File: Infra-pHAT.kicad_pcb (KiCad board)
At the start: 2 copper layers, 65 x 30 mm, 24 parts, among them Q1 BC817, U1 CAT24C32WI-GT3

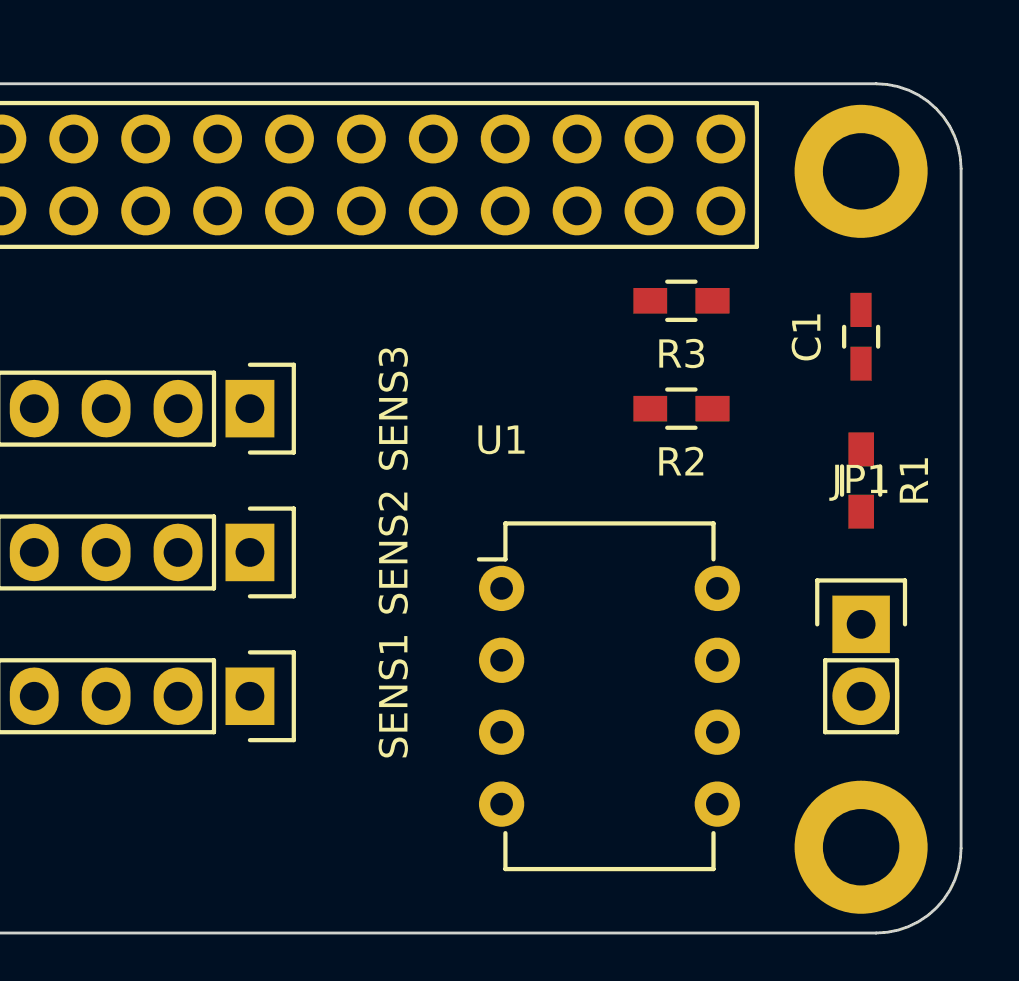
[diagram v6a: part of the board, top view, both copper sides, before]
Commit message: Infra-pHAT.kicad_pcb: Route EEPROM
Signed-off-by: Leon Anavi <leon@anavi.org>
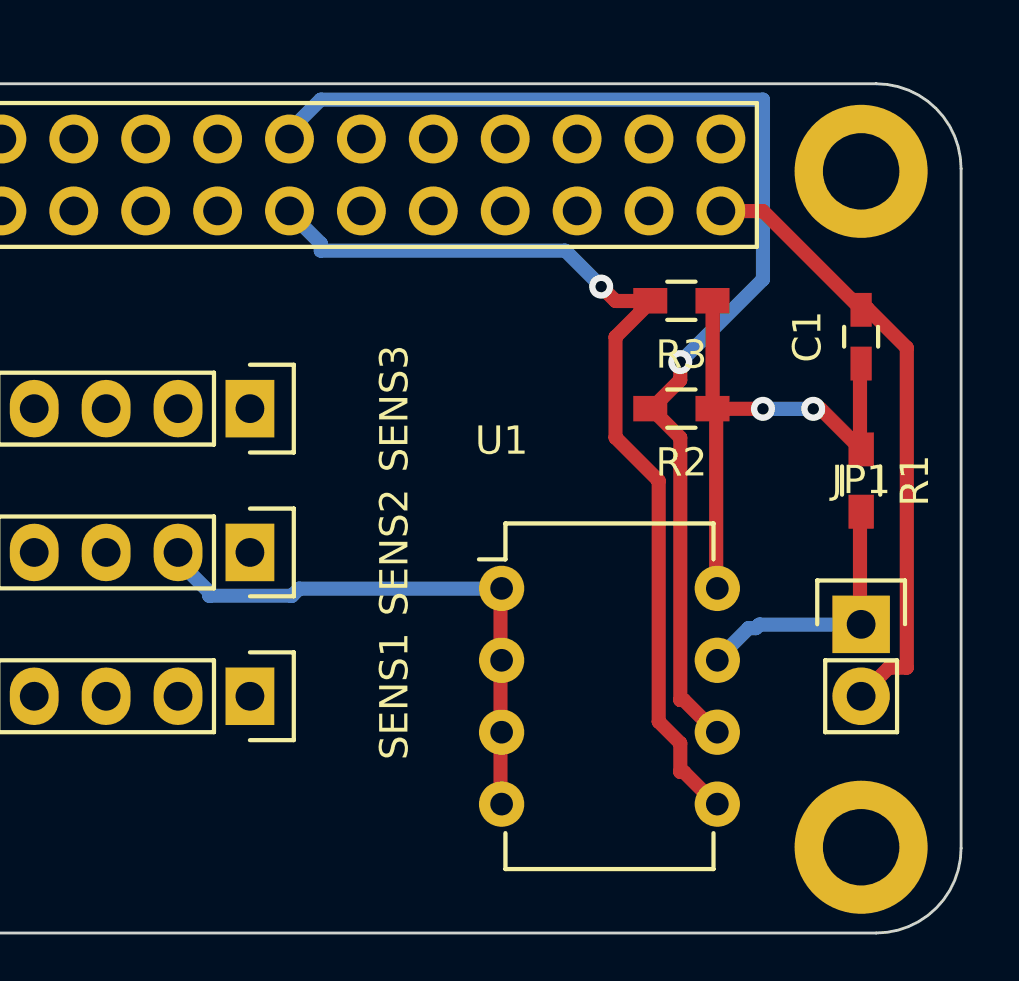
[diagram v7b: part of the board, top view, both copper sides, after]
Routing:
- net Net-(R2-Pad2): track 0.00 -> 42.7 mm, vias 0 -> 1
- net GND: track 0.00 -> 42.5 mm
- net Net-(R3-Pad2): track 0.00 -> 34.3 mm, vias 0 -> 1
- net +3V3: track 0.00 -> 19.3 mm, vias 0 -> 2
- net Net-(JP1-Pad1): track 0.00 -> 9.73 mm
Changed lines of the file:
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@@
   (general
     (links 59)
-    (no_connects 59)
-    (area 136.875429 73.719 225.152572 106.453)
+    (no_connects 43)
+    (area 136.779 73.66 225.171 106.426)
     (thickness 1.6)
     (drawings 13)
-    (tracks 0)
+    (tracks 90)
     (zones 0)
     (modules 24)
@@
   (gr_arc (start 151.5011 102.0036) (end 148.5011 102.0036) (angle -90) (layer Edge.Cuts) (width 0.1))
   (gr_circle (center 152.0011 101.5036) (end 152.0011 101.5036) (layer Edge.Cuts) (width 0.1))
+  (segment (start 204.72 86.48) (end 204.724 86.487) (width 0.5) (layer F.Cu) (net 1) (status 80000))
+  (segment (start 204.724 86.487) (end 204.724 82.677) (width 0.5) (layer F.Cu) (net 1) (status 80000))
+  (segment (start 204.724 82.677) (end 204.72 82.67) (width 0.5) (layer F.Cu) (net 1) (status 80000))
+  (segment (start 204.72 86.48) (end 204.724 86.487) (width 0.5) (layer F.Cu) (net 1) (status 80000))
+  (segment (start 204.724 86.487) (end 206.502 86.487) (width 0.5) (layer F.Cu) (net 1) (status 80000))
+  (via (at 206.502 86.487) (size 0.85) (layers F.Cu B.Cu) (net 1) (status 80000))
+  (segment (start 206.502 86.487) (end 208.28 86.487) (width 0.5) (layer B.Cu) (net 1) (status 80000))
+  (via (at 208.28 86.487) (size 0.85) (layers F.Cu B.Cu) (net 1) (status 80000))
+  (segment (start 208.28 86.487) (end 208.534 86.487) (width 0.5) (layer F.Cu) (net 1) (status 80000))
+  (segment (start 208.534 86.487) (end 209.931 87.884) (width 0.5) (layer F.Cu) (net 1) (status 80000))
+  (segment (start 209.931 87.884) (end 209.97 87.92) (width 0.5) (layer F.Cu) (net 1) (status 80000))
+  (segment (start 209.97 87.92) (end 209.931 87.884) (width 0.5) (layer F.Cu) (net 1) (status 80000))
+  (segment (start 209.931 87.884) (end 209.931 84.836) (width 0.5) (layer F.Cu) (net 1) (status 80000))
+  (segment (start 209.931 84.836) (end 209.97 84.89) (width 0.5) (layer F.Cu) (net 1) (status 80000))
+  (segment (start 204.72 86.48) (end 204.724 86.487) (width 0.5) (layer F.Cu) (net 1) (status 80000))
+  (segment (start 204.724 86.487) (end 204.851 86.614) (width 0.5) (layer F.Cu) (net 1) (status 80000))
+  (segment (start 204.851 86.614) (end 204.851 92.837) (width 0.5) (layer F.Cu) (net 1) (status 80000))
+  (segment (start 204.851 92.837) (end 204.89 92.83) (width 0.5) (layer F.Cu) (net 1) (status 80000))
+  (segment (start 205.017 79.495) (end 204.978 79.502) (width 0.5) (layer F.Cu) (net 2) (status 80000))
+  (segment (start 204.978 79.502) (end 206.502 79.502) (width 0.5) (layer F.Cu) (net 2) (status 80000))
+  (segment (start 206.502 79.502) (end 209.931 82.931) (width 0.5) (layer F.Cu) (net 2) (status 80000))
+  (segment (start 209.931 82.931) (end 209.97 82.99) (width 0.5) (layer F.Cu) (net 2) (status 80000))
+  (segment (start 209.97 82.99) (end 209.931 82.931) (width 0.5) (layer F.Cu) (net 2) (status 80000))
+  (segment (start 209.931 82.931) (end 210.185 82.931) (width 0.5) (layer F.Cu) (net 2) (status 80000))
+  (segment (start 210.185 82.931) (end 211.582 84.328) (width 0.5) (layer F.Cu) (net 2) (status 80000))
+  (segment (start 211.582 84.328) (end 211.582 95.631) (width 0.5) (layer F.Cu) (net 2) (status 80000))
+  (segment (start 211.582 95.631) (end 210.947 95.631) (width 0.5) (layer F.Cu) (net 2) (status 80000))
+  (segment (start 210.947 95.631) (end 209.931 96.647) (width 0.5) (layer F.Cu) (net 2) (status 80000))
+  (segment (start 209.931 96.647) (end 209.97 96.64) (width 0.5) (layer F.Cu) (net 2) (status 80000))
+  (segment (start 185.84 91.56) (end 185.801 91.567) (width 0.5) (layer B.Cu) (net 2) (status 80000))
+  (segment (start 185.801 91.567) (end 185.801 91.821) (width 0.5) (layer B.Cu) (net 2) (status 80000))
+  (segment (start 185.801 91.821) (end 186.944 92.964) (width 0.5) (layer B.Cu) (net 2) (status 80000))
+  (segment (start 186.944 92.964) (end 186.944 93.091) (width 0.5) (layer B.Cu) (net 2) (status 80000))
+  (segment (start 186.944 93.091) (end 189.865 93.091) (width 0.5) (layer B.Cu) (net 2) (status 80000))
+  (segment (start 189.865 93.091) (end 190.119 92.837) (width 0.5) (layer B.Cu) (net 2) (status 80000))
+  (segment (start 190.119 92.837) (end 197.231 92.837) (width 0.5) (layer B.Cu) (net 2) (status 80000))
+  (segment (start 197.231 92.837) (end 197.27 92.83) (width 0.5) (layer B.Cu) (net 2) (status 80000))
+  (segment (start 197.27 97.91) (end 197.231 97.917) (width 0.5) (layer F.Cu) (net 2) (status 80000))
+  (segment (start 197.231 97.917) (end 197.231 100.457) (width 0.5) (layer F.Cu) (net 2) (status 80000))
+  (segment (start 197.231 100.457) (end 197.27 100.45) (width 0.5) (layer F.Cu) (net 2) (status 80000))
+  (segment (start 197.27 95.37) (end 197.231 95.377) (width 0.5) (layer F.Cu) (net 2) (status 80000))
+  (segment (start 197.231 95.377) (end 197.231 97.917) (width 0.5) (layer F.Cu) (net 2) (status 80000))
+  (segment (start 197.231 97.917) (end 197.27 97.91) (width 0.5) (layer F.Cu) (net 2) (status 80000))
+  (segment (start 197.27 92.83) (end 197.231 92.837) (width 0.5) (layer F.Cu) (net 2) (status 80000))
+  (segment (start 197.231 92.837) (end 197.231 95.377) (width 0.5) (layer F.Cu) (net 2) (status 80000))
+  (segment (start 197.231 95.377) (end 197.27 95.37) (width 0.5) (layer F.Cu) (net 2) (status 80000))
+  (segment (start 209.97 94.1) (end 209.931 94.107) (width 0.5) (layer F.Cu) (net 6) (status 80000))
+  (segment (start 209.931 94.107) (end 209.931 90.17) (width 0.5) (layer F.Cu) (net 6) (status 80000))
+  (segment (start 209.931 90.17) (end 209.97 90.12) (width 0.5) (layer F.Cu) (net 6) (status 80000))
+  (segment (start 204.89 95.37) (end 204.851 95.377) (width 0.5) (layer B.Cu) (net 6) (status 80000))
+  (segment (start 204.851 95.377) (end 205.994 94.234) (width 0.5) (layer B.Cu) (net 6) (status 80000))
+  (segment (start 205.994 94.234) (end 206.248 94.234) (width 0.5) (layer B.Cu) (net 6) (status 80000))
+  (segment (start 206.248 94.234) (end 206.375 94.107) (width 0.5) (layer B.Cu) (net 6) (status 80000))
+  (segment (start 206.375 94.107) (end 209.931 94.107) (width 0.5) (layer B.Cu) (net 6) (status 80000))
+  (segment (start 209.931 94.107) (end 209.97 94.1) (width 0.5) (layer B.Cu) (net 6) (status 80000))
+  (segment (start 202.52 86.48) (end 202.565 86.487) (width 0.5) (layer F.Cu) (net 8) (status 80000))
+  (segment (start 202.565 86.487) (end 203.581 85.471) (width 0.5) (layer F.Cu) (net 8) (status 80000))
+  (segment (start 203.581 85.471) (end 203.581 84.836) (width 0.5) (layer F.Cu) (net 8) (status 80000))
+  (via (at 203.581 84.836) (size 0.85) (layers F.Cu B.Cu) (net 8) (status 80000))
+  (segment (start 203.581 84.836) (end 206.502 81.915) (width 0.5) (layer B.Cu) (net 8) (status 80000))
+  (segment (start 206.502 81.915) (end 206.502 75.565) (width 0.5) (layer B.Cu) (net 8) (status 80000))
+  (segment (start 206.502 75.565) (end 190.881 75.565) (width 0.5) (layer B.Cu) (net 8) (status 80000))
+  (segment (start 190.881 75.565) (end 189.738 76.708) (width 0.5) (layer B.Cu) (net 8) (status 80000))
+  (segment (start 189.738 76.708) (end 189.738 76.962) (width 0.5) (layer B.Cu) (net 8) (status 80000))
+  (segment (start 189.738 76.962) (end 189.777 76.955) (width 0.5) (layer B.Cu) (net 8) (status 80000))
+  (segment (start 202.52 86.48) (end 202.565 86.487) (width 0.5) (layer F.Cu) (net 8) (status 80000))
+  (segment (start 202.565 86.487) (end 203.581 87.503) (width 0.5) (layer F.Cu) (net 8) (status 80000))
+  (segment (start 203.581 87.503) (end 203.581 96.774) (width 0.5) (layer F.Cu) (net 8) (status 80000))
+  (segment (start 203.581 96.774) (end 203.708 96.774) (width 0.5) (layer F.Cu) (net 8) (status 80000))
+  (segment (start 203.708 96.774) (end 204.851 97.917) (width 0.5) (layer F.Cu) (net 8) (status 80000))
+  (segment (start 204.851 97.917) (end 204.89 97.91) (width 0.5) (layer F.Cu) (net 8) (status 80000))
+  (segment (start 202.52 82.67) (end 202.565 82.677) (width 0.5) (layer F.Cu) (net 9) (status 80000))
+  (segment (start 202.565 82.677) (end 201.295 82.677) (width 0.5) (layer F.Cu) (net 9) (status 80000))
+  (segment (start 201.295 82.677) (end 200.787 82.169) (width 0.5) (layer F.Cu) (net 9) (status 80000))
+  (via (at 200.787 82.169) (size 0.85) (layers F.Cu B.Cu) (net 9) (status 80000))
+  (segment (start 200.787 82.169) (end 199.517 80.899) (width 0.5) (layer B.Cu) (net 9) (status 80000))
+  (segment (start 199.517 80.899) (end 190.881 80.899) (width 0.5) (layer B.Cu) (net 9) (status 80000))
+  (segment (start 190.881 80.899) (end 190.881 80.645) (width 0.5) (layer B.Cu) (net 9) (status 80000))
+  (segment (start 190.881 80.645) (end 189.738 79.502) (width 0.5) (layer B.Cu) (net 9) (status 80000))
+  (segment (start 189.738 79.502) (end 189.777 79.495) (width 0.5) (layer B.Cu) (net 9) (status 80000))
+  (segment (start 202.52 82.67) (end 202.565 82.677) (width 0.5) (layer F.Cu) (net 9) (status 80000))
+  (segment (start 202.565 82.677) (end 201.295 83.947) (width 0.5) (layer F.Cu) (net 9) (status 80000))
+  (segment (start 201.295 83.947) (end 201.295 87.503) (width 0.5) (layer F.Cu) (net 9) (status 80000))
+  (segment (start 201.295 87.503) (end 202.819 89.027) (width 0.5) (layer F.Cu) (net 9) (status 80000))
+  (segment (start 202.819 89.027) (end 202.819 97.536) (width 0.5) (layer F.Cu) (net 9) (status 80000))
+  (segment (start 202.819 97.536) (end 203.581 98.298) (width 0.5) (layer F.Cu) (net 9) (status 80000))
+  (segment (start 203.581 98.298) (end 203.581 99.314) (width 0.5) (layer F.Cu) (net 9) (status 80000))
+  (segment (start 203.581 99.314) (end 203.708 99.314) (width 0.5) (layer F.Cu) (net 9) (status 80000))
+  (segment (start 203.708 99.314) (end 204.851 100.457) (width 0.5) (layer F.Cu) (net 9) (status 80000))
+  (segment (start 204.851 100.457) (end 204.89 100.45) (width 0.5) (layer F.Cu) (net 9) (status 80000))
 )

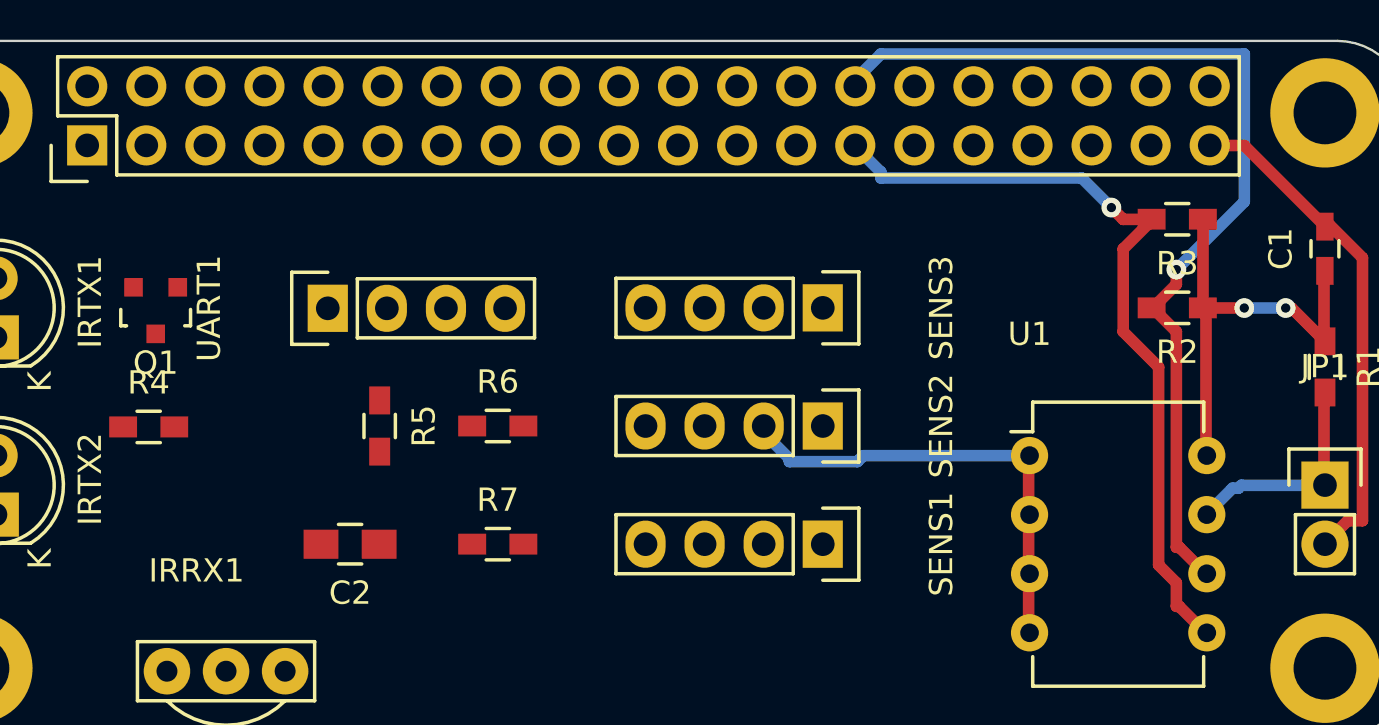
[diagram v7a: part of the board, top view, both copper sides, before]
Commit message: Infra-pHAT.kicad_pcb: Route I2C slots
Signed-off-by: Leon Anavi <leon@anavi.org>
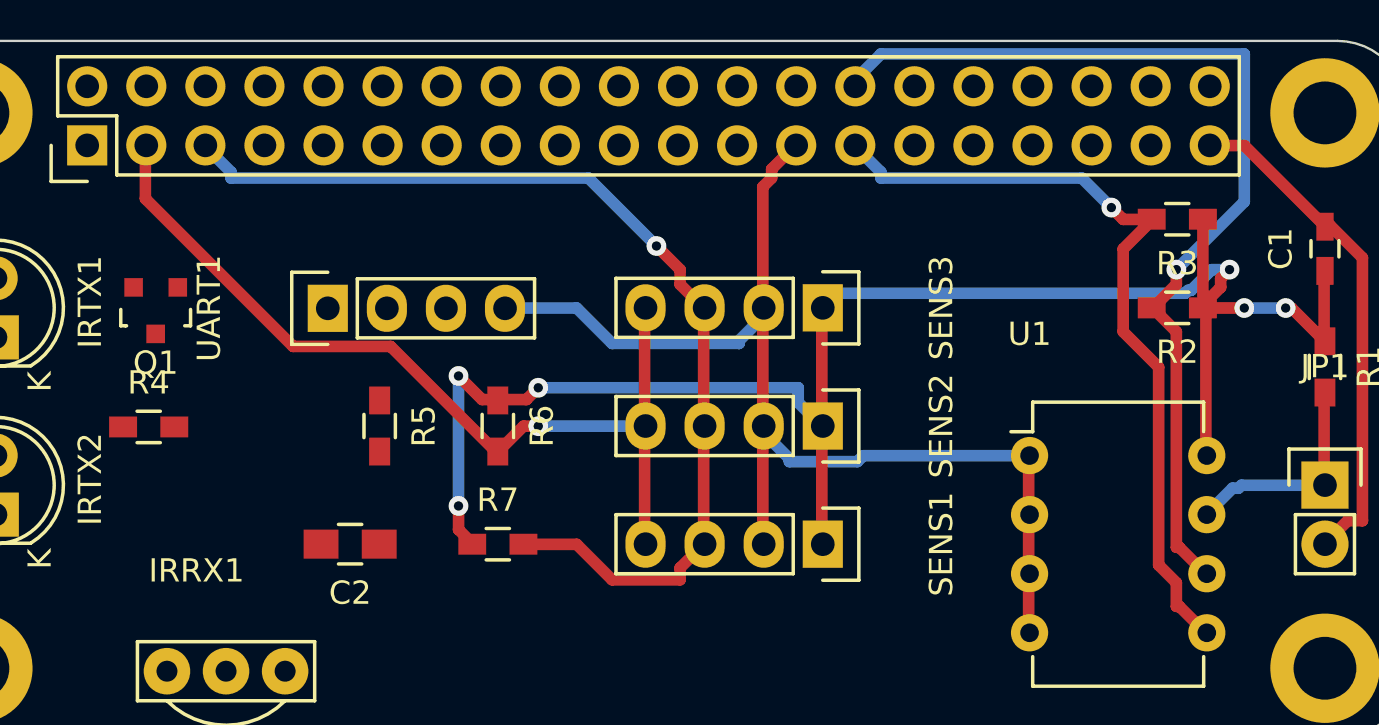
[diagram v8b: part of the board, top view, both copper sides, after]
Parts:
- turned R6 to 270 degrees
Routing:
- net +3V3: track 19.3 -> 75.0 mm, vias 2 -> 6
- net Net-(R7-Pad2): track 0.00 -> 44.6 mm, vias 0 -> 1
- net Net-(R6-Pad2): track 0.00 -> 39.3 mm, vias 0 -> 1
- net GND: track 42.5 -> 73.2 mm
